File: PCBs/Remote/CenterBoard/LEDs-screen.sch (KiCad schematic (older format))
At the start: 25 parts, among them J501 Conn_01x11, U502 TLC555CDR

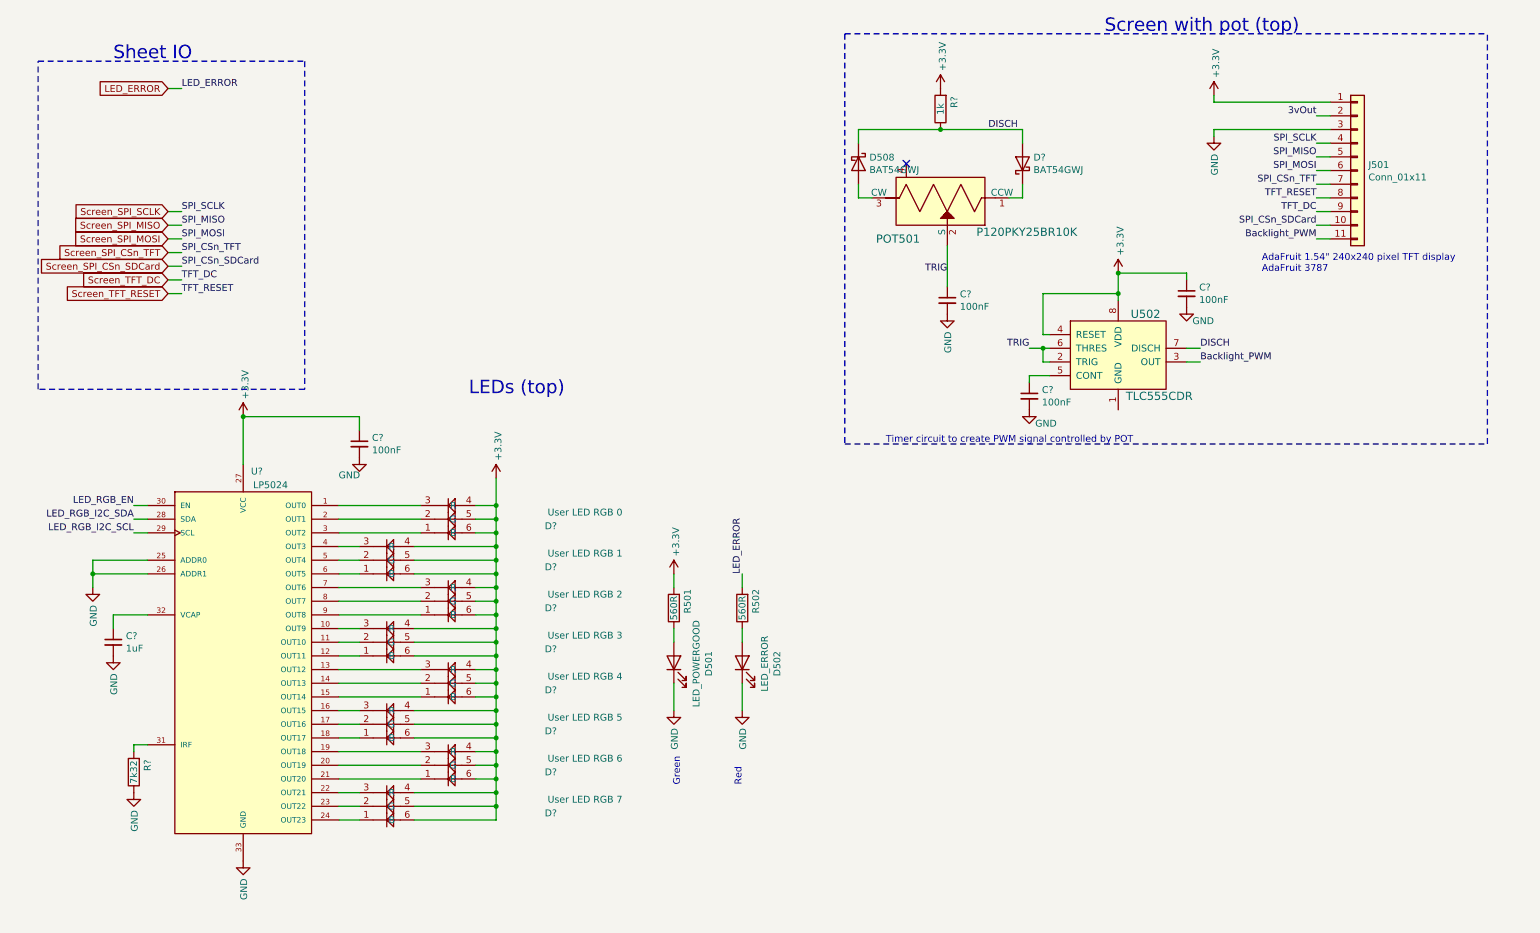
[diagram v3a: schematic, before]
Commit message: Finished leds, redid a lot of PCB wiring. Almost done there now.
Signed-off-by: Eldalote.Electronics <Eldalote.Electronics@gmail.com>
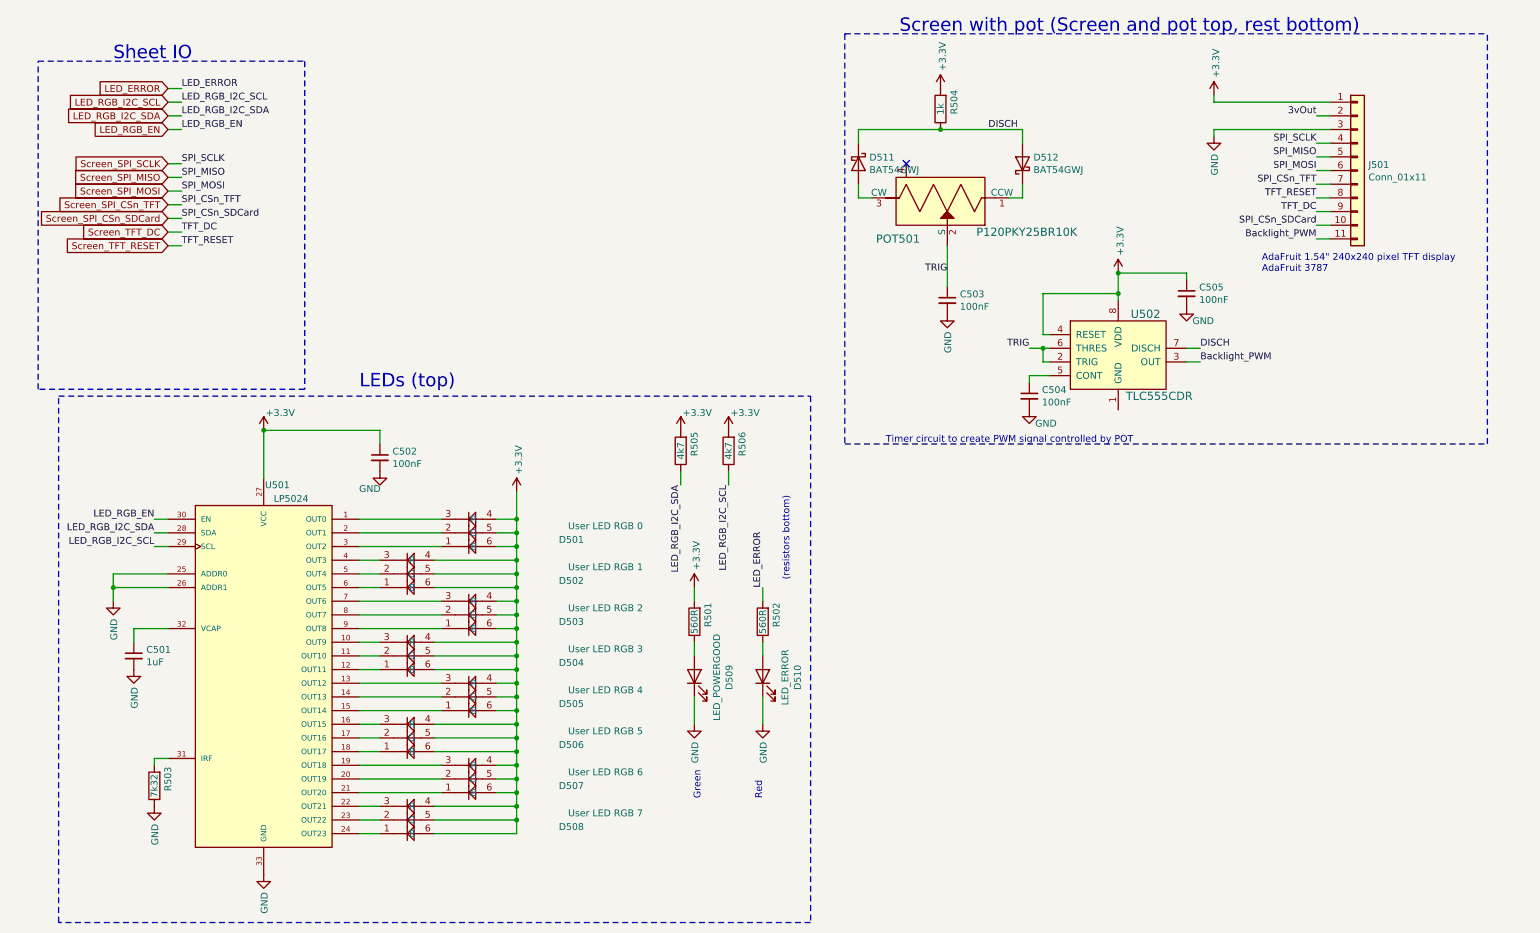
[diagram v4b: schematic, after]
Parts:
- added R505, R506: 4k7, Resistor_SMD:R_0402_1005Metric, symbol Device:R
- C502: renamed from C?; footprint Capacitor_SMD:C_0402_1005Metric -> Capacitor_SMD:C_0805_2012Metric_Pad1.15x1.40mm_HandSolder; DigiKey (none) -> 1276-1099-1-ND; LCSC C1525 -> C49678; Mouser (none) -> 187-CL21B104KACNNNC
- gave numbers to parts that had none: 16
- renumbered D501 to D509, D502 to D510, D508 to D511
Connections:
- net +3V3: now also R505.2, R506.2
- net LED_RGB_I2C_SCL: now also R506.1
- net LED_RGB_I2C_SDA: now also R505.1
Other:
- note added: "(resistors bottom)"
- note added: "Screen with pot (Screen and pot top, rest bottom)"
- note removed: "Screen with pot (top)"
- moved on the sheet: C501, C502, D501, D502, D503, D504, D505, D506, D507, D508, D509, D510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

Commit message: Centerboard v0.1 is done.
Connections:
- net GND: now also U502.1 (GND)
- no-connect marks 1 -> 2
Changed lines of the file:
@@
 Text Label 5600 3900 3    50   ~ 0
 LED_RGB_I2C_SCL
+$Comp
+L power:GND #PWR0109
+U 1 1 5FD86F28
+P 8450 3350
+F 0 "#PWR0109" H 8450 3100 50  0001 C CNN
+F 1 "GND" H 8650 3250 50  0000 R CNN
+F 2 "" H 8450 3350 50  0001 C CNN
+F 3 "" H 8450 3350 50  0001 C CNN
+	1    8450 3350
+	1    0    0    -1
+$EndComp
+NoConn ~ 9900 1200
 $EndSCHEMATC
